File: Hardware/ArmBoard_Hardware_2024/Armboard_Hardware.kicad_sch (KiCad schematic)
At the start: 94 parts, among them J1 RJ45_LED_Shielded, Q1 BSS138, SW1 SW_SPDT, SW10 SW_Push, SW11 SW_Push, SW2 SW_Push, SW3 SW_Push, SW4 SW_Push, SW5 SW_Push, SW6 SW_Push, SW7 SW_Push, SW8 SW_Push, SW9 SW_Push, U1 OKI, U2 Teensy4.1_DEV-16771, U3 74LS148, U4 74LS148, U5 74HC00, U6 OKI

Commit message: Ready for schematic reviews (not)
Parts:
- removed C4, C5: 10uF, Capacitor_SMD:C_0603_1608Metric_Pad1.08x0.95mm_HandSolder, symbol Device:C
- removed U1: OKI, MRDT_Devices:OKI_Horizontal, symbol MRDT_Devices:OKI
- added Conn12, Conn13, Conn14, Conn15, Conn16, Conn17, Conn18, Conn19, Conn20, Conn21, Conn22, Conn23: Molex_SL_04, symbol MRDT_Connectors:Molex_SL_04
- added Conn24, Conn25, Conn26: Molex_SL_03, symbol MRDT_Connectors:Molex_SL_03
- added V1, V2, V3, V4: Via, MRDT_Drill_Holes:4_40_Hole_Corner, symbol MRDT_Drill_Holes:Via
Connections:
- net +3V3: now also Conn20.1, Conn21.1, Conn22.1, Conn23.1, Conn24.1, Conn25.1
- net +5V: now also U2.5V, Conn12.1, Conn13.1, Conn14.1, Conn15.1, Conn16.1, Conn17.1, Conn18.1, Conn19.1, Conn26.1
- net GND: now also Conn12.4, Conn13.4, Conn14.4, Conn15.4, Conn16.4, Conn17.4, Conn18.4, Conn19.4, Conn20.4, Conn21.4, Conn22.4, Conn23.4, Conn24.3, Conn25.3, Conn26.3
- net LAS: now also U2.23 (A9)
- net AbsEncoder2: now reaches U2.11 (MOSI)
- net AbsEncoder2: now also Conn24.2
- net AbsEncoder1: now reaches U2.12 (MISO)
- net AbsEncoder1: now also Conn25.2
- net MOCO3_FWD: now reaches U2.18 (A4)
- net MOCO3_FWD: now also Conn17.2
- net MOCO3_RVS: now reaches U2.19 (A5)
- net MOCO3_RVS: now also Conn17.3
- net MOCO6_FWD: now reaches U2.2 (OUT2)
- net MOCO6_FWD: now also Conn14.2
- net MOCO4_FWD: now reaches U2.20 (A6)
- net MOCO4_FWD: now also Conn13.2
- net MOCO4_RVS: now reaches U2.21 (A7)
- net MOCO4_RVS: now also Conn13.3
- net Encoder4B: now reaches U2.24 (A10)
- net Encoder4B: now also Conn22.3
- net Encoder4A: now reaches U2.25 (A11)
- net Encoder4A: now also Conn22.2
- net Encoder3B: now reaches U2.26 (A12)
- net Encoder3B: now also Conn23.3
- net Encoder3A: now reaches U2.27 (A13)
- net Encoder3A: now also Conn23.2
- net MOCO2_FWD: now reaches U2.3 (LRCLK2)
- net MOCO2_FWD: now also Conn12.2
- net MOCO1_FWD: now reaches U2.30 (CRX3)
- net MOCO1_FWD: now also Conn16.2
- net MOCO1_RVS: now reaches U2.31 (CTX3)
- net MOCO1_RVS: now also Conn16.3
- net MOCO7_RVS: now reaches U2.32 (OUT1B)
- net MOCO7_RVS: now also Conn19.3
- net MOCO8_RVS: now reaches U2.36 (CS2)
- net MOCO8_RVS: now also Conn15.3
- net MOCO8_FWD: now reaches U2.37 (CS3)
- net MOCO8_FWD: now also Conn15.2
- net Encoder2B: now reaches U2.38 (A14)
- net Encoder2B: now also Conn20.3
- net Encoder2A: now reaches U2.39 (A15)
- net Encoder2A: now also Conn20.2
- net MOCO2_RVS: now reaches U2.4 (BCLK2)
- net MOCO2_RVS: now also Conn12.3
- net Encoder1B: now reaches U2.40 (A16)
- net Encoder1B: now also Conn21.3
- net Encoder1A: now reaches U2.41 (A17)
- net Encoder1A: now also Conn21.2
- net MOCO6_RVS: now reaches U2.6 (OUT1D)
- net MOCO6_RVS: now also Conn14.3
- net MOCO7_FWD: now reaches U2.9 (OUT1C)
- net MOCO7_FWD: now also Conn19.2
- net MOCO5_RVS: now reaches U2.D (D-)
- net MOCO5_RVS: now also Conn18.3
- net MOCO5_FWD: now reaches U2.D+
- net MOCO5_FWD: now also Conn18.2
- new net Servo: Conn26.2
- no-connect marks 42 -> 14
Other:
- note added: "BUTTON 16:4 ENCODER"
- note added: "BUTTONS"
- note added: "ENCODERS"
- note added: "LASERS"
- note added: "Limit Switches"
- note added: "MOCOS"
- note added: "MOUNTS"
- note added: "POWER"
- moved on the sheet: C6, C7, C8, D10, D11, D12, D13, D3, D4, D5, D6, D7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

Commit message: Post schematic review
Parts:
- removed C1: 470uF, symbol Device:C
- removed C2: 220uF, symbol Device:C
- removed C3: 100uF, symbol Device:C
- added C4, C5: 10uF, Capacitor_SMD:C_0603_1608Metric_Pad1.08x0.95mm_HandSolder, symbol Device:C
- added U1: OKI, MRDT_Devices:OKI_Horizontal, symbol MRDT_Devices:OKI
- R1: value 3k -> 1k
- renumbered D3 to D14, D14 to D23
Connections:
- net +3V3 is gone; now on net +3.3V: Conn2.1, Conn20.1, Conn21.1, Conn22.1, Conn23.1, Conn24.1, Conn25.1, Conn3.1, Conn4.1, Conn5.1, Conn6.1, Conn7.1, Conn8.1, Conn9.1, D10.2 (A), D11.2 (A), D12.2 (A), D13.2 (A), D14.2 (A), D4.2 (A), D5.2 (A), D6.2 (A), D7.2 (A), D8.2 (A), D9.2 (A), R10.1, R11.1, R12.1, R16.1, R17.1, R18.1, R22.1, R4.1, R5.1, R6.1, SW1.1 (A)
- net +12V: now also C4.1, U1.1 (Vi)
- net +3.3V: now also Conn12.1, Conn13.1, Conn14.1, Conn15.1, Conn16.1, Conn17.1, Conn18.1, Conn19.1, C5.1, U1.3 (Vo); no longer U2.3.3V_1 (3.3V), U2.3.3V_2 (3.3V), U2.3.3V_3 (3.3V)
- net +5V: now also U2.VIN; no longer Conn12.1, Conn13.1, Conn14.1, Conn15.1, Conn16.1, Conn17.1, Conn18.1, Conn19.1, U2.5V
- net DIR_SW: now also U2.21 (A7); no longer U2.13 (SCK)
- net GND: now also C4.2, C5.2, U1.2 (GND)
- net LIM_1: now also U2.D (D-); no longer U2.0 (RX1)
- net LIM_2: now also U2.D+; no longer U2.1 (TX1)
- net LIM_3: now also U2.28 (RX7); no longer U2.7 (RX2)
- net LIM_4: now also U2.29 (TX7); no longer U2.8 (TX2)
- net LIM_5: now also U2.34 (RX8); no longer U2.28 (RX7)
- net LIM_6: now also U2.35 (TX8); no longer U2.29 (TX7)
- net LIM_7: now also U2.30 (CRX3); no longer U2.34 (RX8)
- net LIM_8: now also U2.31 (CTX3); no longer U2.35 (TX8)
- net MOCO1_FWD: now also U2.0 (RX1); no longer U2.30 (CRX3)
- net MOCO1_RVS: now also U2.1 (TX1); no longer U2.31 (CTX3)
- net MOCO3_FWD: now also U2.33 (MCLK2); no longer U2.18 (A4)
- net MOCO3_RVS: now also U2.13 (SCK); no longer U2.19 (A5)
- net MOCO4_FWD: now also U2.18 (A4); no longer U2.20 (A6)
- net MOCO4_RVS: now also U2.19 (A5); no longer U2.21 (A7)
- net MOCO5_FWD: now also U2.8 (TX2); no longer U2.D+
- net MOCO5_RVS: now also U2.7 (RX2); no longer U2.D (D-)
- net MOCO7_RVS: now also U2.22 (A8); no longer U2.32 (OUT1B)
- net Servo: now also U2.20 (A6)
- new net: U2.3.3V_1 (3.3V), U2.3.3V_2 (3.3V), U2.3.3V_3 (3.3V)
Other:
- note added: "SERVO"
- moved on the sheet: Conn26, D10, D11, D12, D13, D14, D4, D5, D6, D7, D8, D9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

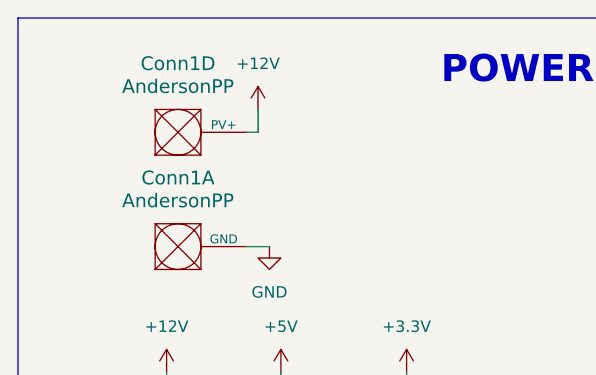
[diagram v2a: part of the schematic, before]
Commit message: Changed Anderson to V+ Log instead of V+ Act
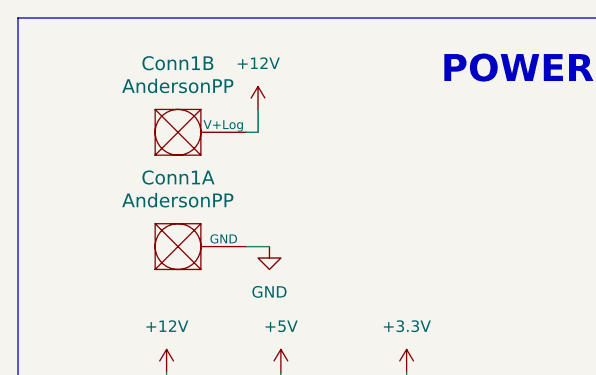
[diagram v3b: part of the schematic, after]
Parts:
- removed unit 4 of Conn1
- added unit 2 of Conn1
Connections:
- net +12V: now also Conn1.2 (V+Log)
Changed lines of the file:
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@@
-    )
-  )
-  (symbol (lib_id "MRDT_Connectors:AndersonPP") (at 27.94 27.94 0) (unit 4)
-    (in_bom yes) (on_board yes) (dnp no) (fields_autoplaced)
-    (property "Reference" "Conn1" (at 30.48 17.78 0)
-      (effects (font (size 1.524 1.524)))
-    )
-    (property "Value" "AndersonPP" (at 30.48 20.32 0)
-      (effects (font (size 1.524 1.524)))
-    )
-    (property "Footprint" "MRDT_Connectors:Square_Anderson_2_H_Side_By_Side_PV" (at 24.13 41.91 0)
-      (effects (font (size 1.524 1.524)) hide)
-    )
-    (property "Datasheet" "" (at 24.13 41.91 0)
-      (effects (font (size 1.524 1.524)) hide)
-    )
-    (pin "1")
-    (pin "2")
-    (pin "3")
-    (pin "4")
-    (pin "1")
-    (instances
-      (project "Armboard_Hardware"
-        (path "/0313b944-1194-481e-8200-b9ebb32d70a5"
-          (reference "Conn1") (unit 4)
-        )
-      )
-      (project "Ethan_Daly"
-        (path "/fae4b32c-b8f2-4caa-8bb4-00877803f589"
-          (reference "Conn1") (unit 4)
-        )
-      )
     )
   )
@@
         )
       )
+    )
+  )
+  (symbol (lib_id "MRDT_Connectors:AndersonPP") (at 27.94 27.94 0) (unit 2)
+    (in_bom yes) (on_board yes) (dnp no) (fields_autoplaced)
+    (property "Reference" "Conn1" (at 30.48 17.78 0)
+      (effects (font (size 1.524 1.524)))
+    )
+    (property "Value" "AndersonPP" (at 30.48 20.32 0)
+      (effects (font (size 1.524 1.524)))
+    )
+    (property "Footprint" "" (at 24.13 41.91 0)
+      (effects (font (size 1.524 1.524)) hide)
+    )
+    (property "Datasheet" "" (at 24.13 41.91 0)
+      (effects (font (size 1.524 1.524)) hide)
+    )
+    (pin "1")
+    (pin "2")
+    (pin "3")
+    (pin "4")
+    (pin "1")
+    (instances
+      (project "Armboard_Hardware"
+        (path "/0313b944-1194-481e-8200-b9ebb32d70a5"
+          (reference "Conn1") (unit 2)
+        )
+      )

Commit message: layout spaced components
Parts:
- Conn1: footprint MRDT_Connectors:Square_Anderson_2_H_Side_By_Side_PV -> MRDT_Connectors:Square_Anderson_2_H_Side_By_Side
- Conn1: footprint (none) -> MRDT_Connectors:Square_Anderson_2_H_Side_By_Side
- Conn12, Conn13, Conn14, Conn15, Conn16, Conn17, Conn18, Conn19, Conn20, Conn21, Conn22, Conn23: footprint (none) -> MRDT_Connectors:MOLEX_SL_04_Vertical
- Conn24, Conn25, Conn26: footprint (none) -> MRDT_Connectors:MOLEX_SL_03_Vertical
- U3, U4: footprint (none) -> Package_SO:SOIC-16_3.9x9.9mm_P1.27mm
- U5: footprint (none) -> Package_SO:SO-14_3.9x8.65mm_P1.27mm
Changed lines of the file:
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@@
       (effects (font (size 1.27 1.27)) (justify left))
     )
-    (property "Footprint" "" (at 59.69 134.62 0)
+    (property "Footprint" "Package_SO:SO-14_3.9x8.65mm_P1.27mm" (at 59.69 134.62 0)
       (effects (font (size 1.27 1.27)) hide)
     )
@@
       (effects (font (size 1.524 1.524)) (justify left))
     )
-    (property "Footprint" "" (at 387.35 223.52 0)
+    (property "Footprint" "MRDT_Connectors:MOLEX_SL_04_Vertical" (at 387.35 223.52 0)
       (effects (font (size 1.524 1.524)) hide)
     )
@@
       (effects (font (size 1.27 1.27)) (justify left))
     )
-    (property "Footprint" "" (at 22.86 120.65 0)
+    (property "Footprint" "Package_SO:SO-14_3.9x8.65mm_P1.27mm" (at 22.86 120.65 0)
       (effects (font (size 1.27 1.27)) hide)
     )
@@
       (effects (font (size 1.524 1.524)) (justify left))
     )
-    (property "Footprint" "" (at 346.71 200.66 0)
+    (property "Footprint" "MRDT_Connectors:MOLEX_SL_04_Vertical" (at 346.71 200.66 0)
       (effects (font (size 1.524 1.524)) hide)
     )
@@
       (effects (font (size 1.27 1.27)) (justify left))
     )
-    (property "Footprint" "" (at 76.2 134.62 0)
+    (property "Footprint" "Package_SO:SO-14_3.9x8.65mm_P1.27mm" (at 76.2 134.62 0)
       (effects (font (size 1.27 1.27)) hide)
     )
@@
       (effects (font (size 1.524 1.524)) (justify left))
     )
-    (property "Footprint" "" (at 264.16 179.07 0)
+    (property "Footprint" "MRDT_Connectors:MOLEX_SL_04_Vertical" (at 264.16 179.07 0)
       (effects (font (size 1.524 1.524)) hide)
     )
@@
       (effects (font (size 1.524 1.524)) (justify left))
     )
-    (property "Footprint" "" (at 302.26 200.66 0)
+    (property "Footprint" "MRDT_Connectors:MOLEX_SL_04_Vertical" (at 302.26 200.66 0)
       (effects (font (size 1.524 1.524)) hide)
     )
@@
       (effects (font (size 1.524 1.524)) (justify left))
     )
-    (property "Footprint" "" (at 262.89 222.25 0)
+    (property "Footprint" "MRDT_Connectors:MOLEX_SL_03_Vertical" (at 262.89 222.25 0)
       (effects (font (size 1.524 1.524)) hide)
     )
@@
       (effects (font (size 1.524 1.524)) (justify left))
     )
-    (property "Footprint" "" (at 387.35 200.66 0)
+    (property "Footprint" "MRDT_Connectors:MOLEX_SL_04_Vertical" (at 387.35 200.66 0)
       (effects (font (size 1.524 1.524)) hide)
     )
@@
       (effects (font (size 1.524 1.524)) (justify left))
     )
-    (property "Footprint" "" (at 346.71 177.8 0)
+    (property "Footprint" "MRDT_Connectors:MOLEX_SL_04_Vertical" (at 346.71 177.8 0)
       (effects (font (size 1.524 1.524)) hide)
     )
@@
       (effects (font (size 1.524 1.524)) (justify left))
     )
-    (property "Footprint" "" (at 278.13 275.59 0)
+    (property "Footprint" "MRDT_Connectors:MOLEX_SL_03_Vertical" (at 278.13 275.59 0)
       (effects (font (size 1.524 1.524)) hide)
     )
@@
       (effects (font (size 1.524 1.524)) (justify left))
     )
-    (property "Footprint" "" (at 346.71 223.52 0)
+    (property "Footprint" "MRDT_Connectors:MOLEX_SL_04_Vertical" (at 346.71 223.52 0)
       (effects (font (size 1.524 1.524)) hide)
     )
@@
       (effects (font (size 1.524 1.524)) (justify left))
     )
-    (property "Footprint" "" (at 302.26 179.07 0)
+    (property "Footprint" "MRDT_Connectors:MOLEX_SL_04_Vertical" (at 302.26 179.07 0)
       (effects (font (size 1.524 1.524)) hide)
     )
@@
       (effects (font (size 1.524 1.524)) (justify left))
     )
-    (property "Footprint" "" (at 387.35 177.8 0)
+    (property "Footprint" "MRDT_Connectors:MOLEX_SL_04_Vertical" (at 387.35 177.8 0)
       (effects (font (size 1.524 1.524)) hide)
     )
@@
       (effects (font (size 1.27 1.27)))
     )
-    (property "Footprint" "" (at 48.26 106.68 0)
+    (property "Footprint" "Package_SO:SOIC-16_3.9x9.9mm_P1.27mm" (at 48.26 106.68 0)
       (effects (font (size 1.27 1.27)) hide)
     )
@@
       (effects (font (size 1.27 1.27)) (justify left))
     )
-    (property "Footprint" "" (at 40.64 134.62 0)
+    (property "Footprint" "Package_SO:SO-14_3.9x8.65mm_P1.27mm" (at 40.64 134.62 0)
       (effects (font (size 1.27 1.27)) hide)
     )
@@
       (effects (font (size 1.524 1.524)) (justify left))
     )
-    (property "Footprint" "" (at 346.71 246.38 0)
+    (property "Footprint" "MRDT_Connectors:MOLEX_SL_04_Vertical" (at 346.71 246.38 0)
       (effects (font (size 1.524 1.524)) hide)
     )
@@
       (effects (font (size 1.524 1.524)) (justify left))
     )
-    (property "Footprint" "" (at 387.35 246.38 0)
+    (property "Footprint" "MRDT_Connectors:MOLEX_SL_04_Vertical" (at 387.35 246.38 0)
       (effects (font (size 1.524 1.524)) hide)
     )
@@
       (effects (font (size 1.524 1.524)) (justify left))
     )
-    (property "Footprint" "" (at 303.53 222.25 0)
+    (property "Footprint" "MRDT_Connectors:MOLEX_SL_03_Vertical" (at 303.53 222.25 0)
       (effects (font (size 1.524 1.524)) hide)
     )
@@
       (effects (font (size 1.27 1.27)) (justify left))
     )
-    (property "Footprint" "" (at 92.71 134.62 0)
+    (property "Footprint" "Package_SO:SO-14_3.9x8.65mm_P1.27mm" (at 92.71 134.62 0)
       (effects (font (size 1.27 1.27)) hide)
     )
@@
       (effects (font (size 1.524 1.524)))
     )
-    (property "Footprint" "MRDT_Connectors:Square_Anderson_2_H_Side_By_Side_PV" (at 24.13 54.61 0)
+    (property "Footprint" "MRDT_Connectors:Square_Anderson_2_H_Side_By_Side" (at 24.13 54.61 0)
       (effects (font (size 1.524 1.524)) hide)
     )
@@
       (effects (font (size 1.524 1.524)) (justify left))
     )
-    (property "Footprint" "" (at 264.16 200.66 0)
+    (property "Footprint" "MRDT_Connectors:MOLEX_SL_04_Vertical" (at 264.16 200.66 0)
       (effects (font (size 1.524 1.524)) hide)
     )
@@
       (effects (font (size 1.524 1.524)))
     )
-    (property "Footprint" "" (at 24.13 41.91 0)
+    (property "Footprint" "MRDT_Connectors:Square_Anderson_2_H_Side_By_Side" (at 24.13 41.91 0)
       (effects (font (size 1.524 1.524)) hide)
     )
@@
       (effects (font (size 1.27 1.27)))
     )
-    (property "Footprint" "" (at 92.71 106.68 0)
+    (property "Footprint" "Package_SO:SOIC-16_3.9x9.9mm_P1.27mm" (at 92.71 106.68 0)
       (effects (font (size 1.27 1.27)) hide)
     )

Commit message: traces finished
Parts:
- removed Conn12, Conn13, Conn14, Conn15, Conn16, Conn17, Conn18, Conn19: Molex_SL_04, MRDT_Connectors:MOLEX_SL_04_Vertical, symbol MRDT_Connectors:Molex_SL_04
- added Conn12, Conn13, Conn14, Conn15, Conn16, Conn17, Conn18, Conn19: Molex_SL_03, MRDT_Connectors:MOLEX_SL_03_Vertical, symbol MRDT_Connectors:Molex_SL_03
- R13, R14, R15, R19, R2, R20, R21, R23, R25, R26, R27, R28, R29, R3, R30, R31, R32, R7, R8, R9: value 120 -> 100
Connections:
- net +3.3V: now also Conn12.1, Conn13.1, Conn14.1, Conn15.1, Conn16.1, Conn17.1, Conn18.1, Conn19.1
- net AbsEncoder1: now also U2.24 (A10); no longer U2.12 (MISO)
- net AbsEncoder2: now also U2.12 (MISO); no longer U2.11 (MOSI)
- net B_ENC_0: now also U2.16 (A2); no longer U2.14 (A0)
- net B_ENC_1: now also U2.17 (A3); no longer U2.15 (A1)
- net B_ENC_2: now also U2.20 (A6); no longer U2.16 (A2)
- net B_ENC_3: now also U2.21 (A7); no longer U2.17 (A3)
- net DIR_SW: now also U2.33 (MCLK2); no longer U2.21 (A7)
- net Encoder1A: now also U2.32 (OUT1B); no longer U2.41 (A17)
- net Encoder1B: now also U2.31 (CTX3); no longer U2.40 (A16)
- net Encoder2A: now also U2.30 (CRX3); no longer U2.39 (A15)
- net Encoder2B: now also U2.29 (TX7); no longer U2.38 (A14)
- net Encoder3A: now also U2.28 (RX7); no longer U2.27 (A13)
- net Encoder3B: now also U2.27 (A13); no longer U2.26 (A12)
- net Encoder4A: now also U2.26 (A12); no longer U2.25 (A11)
- net Encoder4B: now also U2.25 (A11); no longer U2.24 (A10)
- net LAS: now also U2.22 (A8); no longer U2.23 (A9)
- net LIM_1: now also U2.34 (RX8); no longer U2.D (D-)
- net LIM_2: now also U2.35 (TX8); no longer U2.D+
- net LIM_3: now also U2.36 (CS2); no longer U2.28 (RX7)
- net LIM_4: now also U2.37 (CS3); no longer U2.29 (TX7)
- net LIM_5: now also U2.38 (A14); no longer U2.34 (RX8)
- net LIM_6: now also U2.39 (A15); no longer U2.35 (TX8)
- net LIM_7: now also U2.40 (A16); no longer U2.30 (CRX3)
- net LIM_8: now also U2.41 (A17); no longer U2.31 (CTX3)
- net MOCO1_FWD: now also U2.14 (A0), Conn12.2; no longer U2.0 (RX1)
- net MOCO1_RVS: now also U2.15 (A1), Conn12.3; no longer U2.1 (TX1)
- net MOCO2_FWD: now also U2.9 (OUT1C), Conn13.2; no longer U2.3 (LRCLK2)
- net MOCO2_RVS: now also U2.8 (TX2), Conn13.3; no longer U2.4 (BCLK2)
- net MOCO3_FWD: now also U2.5 (IN2), Conn14.2; no longer U2.33 (MCLK2)
- net MOCO3_RVS: now also U2.4 (BCLK2), Conn14.3; no longer U2.13 (SCK)
- net MOCO4_FWD: now also U2.1 (TX1), Conn15.2; no longer U2.18 (A4)
- net MOCO4_RVS: now also U2.0 (RX1), Conn15.3; no longer U2.19 (A5)
- net MOCO5_FWD: now also U2.2 (OUT2), Conn16.2; no longer U2.8 (TX2)
- net MOCO5_RVS: now also U2.3 (LRCLK2), Conn16.3; no longer U2.7 (RX2)
- net MOCO6_FWD: now also U2.6 (OUT1D), Conn17.2; no longer U2.2 (OUT2)
- net MOCO6_RVS: now also U2.7 (RX2), Conn17.3; no longer U2.6 (OUT1D)
- net MOCO7_FWD: now also U2.10 (CS1), Conn18.2; no longer U2.9 (OUT1C)
- net MOCO7_RVS: now also U2.11 (MOSI), Conn18.3; no longer U2.22 (A8)
- net MOCO8_FWD: now also U2.19 (A5), Conn19.2; no longer U2.37 (CS3)
- net MOCO8_RVS: now also U2.18 (A4), Conn19.3; no longer U2.36 (CS2)
- net Servo: now also U2.23 (A9); no longer U2.20 (A6)

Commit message: layout review 2
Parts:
- Conn10, Conn11, Conn2, Conn3, Conn4, Conn5, Conn6, Conn7, Conn8, Conn9: footprint Connector_Molex:Molex_SL_171971-0002_1x02_P2.54mm_Vertical -> MRDT_Connectors:MOLEX_SL_02_Horizontal
- Conn20, Conn21, Conn22, Conn23: footprint MRDT_Connectors:MOLEX_SL_04_Vertical -> MRDT_Connectors:MOLEX_SL_04_Horizontal
- Conn24, Conn25: footprint MRDT_Connectors:MOLEX_SL_03_Vertical -> MRDT_Connectors:MOLEX_SL_03_Horizontal
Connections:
- net AbsEncoder1: now also Conn24.2, U2.32 (OUT1B); no longer Conn25.2, U2.24 (A10)
- net AbsEncoder2: now also Conn25.2, U2.31 (CTX3); no longer Conn24.2, U2.12 (MISO)
- net B_2: now also R5.2, R8.2, SW3.2; no longer R10.2, R13.2, SW5.2
- net B_3: now also R6.2, R9.2, SW4.2; no longer R16.2, R19.2, SW8.2
- net B_4: now also R10.2, R13.2, SW5.2; no longer R5.2, R8.2, SW3.2
- net B_6: now also R12.2, R15.2, SW7.2; no longer R17.2, R20.2, SW9.2
- net B_7: now also R16.2, R19.2, SW8.2; no longer R6.2, R9.2, SW4.2
- net B_8: now also R17.2, R20.2, SW9.2; no longer R12.2, R15.2, SW7.2
- net B_ENC_0: now also U2.21 (A7); no longer U2.16 (A2)
- net B_ENC_1: now also U2.20 (A6); no longer U2.17 (A3)
- net B_ENC_2: now also U2.17 (A3); no longer U2.20 (A6)
- net B_ENC_3: now also U2.16 (A2); no longer U2.21 (A7)
- net Encoder1A: now also Conn20.2, U2.30 (CRX3); no longer Conn21.2, U2.32 (OUT1B)
- net Encoder1B: now also Conn20.3, U2.29 (TX7); no longer Conn21.3, U2.31 (CTX3)
- net Encoder2A: now also Conn21.2, U2.28 (RX7); no longer Conn20.2, U2.30 (CRX3)
- net Encoder2B: now also Conn21.3, U2.27 (A13); no longer Conn20.3, U2.29 (TX7)
- net Encoder3A: now also Conn22.2, U2.26 (A12); no longer Conn23.2, U2.28 (RX7)
- net Encoder3B: now also Conn22.3, U2.25 (A11); no longer Conn23.3, U2.27 (A13)
- net Encoder4A: now also Conn23.2, U2.24 (A10); no longer Conn22.2, U2.26 (A12)
- net Encoder4B: now also Conn23.3, U2.12 (MISO); no longer Conn22.3, U2.25 (A11)
- net LIM_2: now also Conn3.2; no longer Conn4.2
- net LIM_3: now also Conn4.2; no longer Conn6.2
- net LIM_4: now also Conn5.2; no longer Conn3.2
- net LIM_5: now also Conn6.2; no longer Conn5.2
- net MOCO1_FWD: now also U2.15 (A1); no longer U2.14 (A0)
- net MOCO1_RVS: now also U2.14 (A0); no longer U2.15 (A1)
- net MOCO8_FWD: now also U2.18 (A4); no longer U2.19 (A5)
- net MOCO8_RVS: now also U2.19 (A5); no longer U2.18 (A4)
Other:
- moved on the sheet: Conn20, Conn21, Conn22, Conn23, Conn24, Conn25, Conn3, Conn4, Conn5, Conn6

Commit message: final layout for orders
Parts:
- Conn26: footprint MRDT_Connectors:MOLEX_SL_03_Vertical -> MRDT_Connectors:MOLEX_SL_03_Horizontal
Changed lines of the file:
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@@
       (effects (font (size 1.524 1.524)) (justify left))
     )
-    (property "Footprint" "MRDT_Connectors:MOLEX_SL_03_Vertical" (at 278.13 275.59 0)
+    (property "Footprint" "MRDT_Connectors:MOLEX_SL_03_Horizontal" (at 278.13 275.59 0)
       (effects (font (size 1.524 1.524)) hide)
     )
